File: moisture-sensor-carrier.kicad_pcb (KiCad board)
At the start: 4 copper layers, 42 x 155 mm, 61 parts, among them J1 USB-C receptacle, J2 Battery - Adafruit 1578, J3 Solar panel, J4 SWD 10p 1.27mm, J5 U.FL-R-SMT-1(10) antenna, U1 nRF54L15-QFAA, U2 nPM1300-QEAA, U3 FDC1004, U4 SHT45-AD1F, U5 TPS7A1650 5V LDO, X1 CM8V-T1A 32.768kHz CL=7pF 20p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, X2 FA-128 32MHz CL=8pF

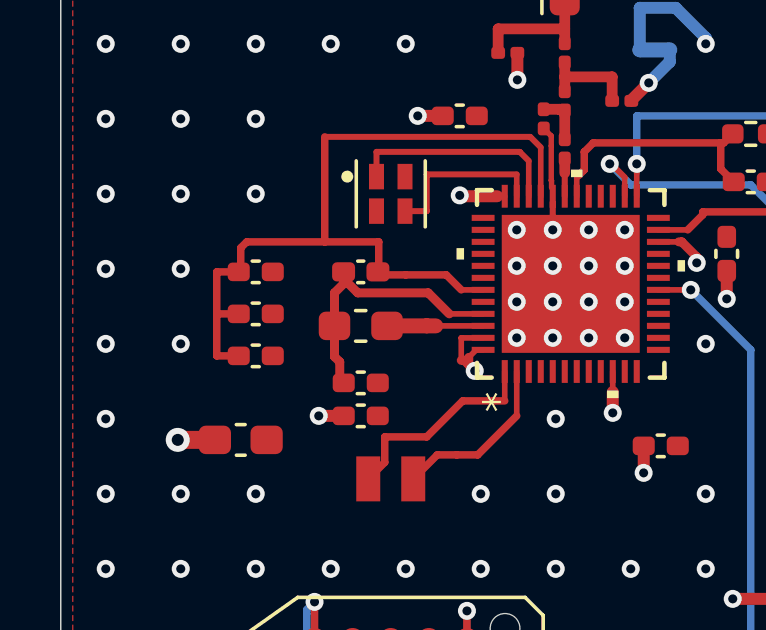
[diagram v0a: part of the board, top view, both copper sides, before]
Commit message: Pull the DECA bank in and give the decoupling local ground returns
Half the DECA bank's distance was free: C2, C12 and C5 all had their /DECA pad
on the WEST side, pointing AWAY from U1, so the net left each capacitor going
the wrong direction and doubled back. 1.13 mm each, for a rotation.

    C2   8.17 -> 6.04 mm      C12  8.19 -> 6.59      C5  8.44 -> 6.90

The eastward shift on top of that is small, and the reason is worth stating
rather than filing as a nudge: the band between the bank and the FB1/L1 column
is 0.67 mm, so each cap moved until its courtyard met its neighbour with
0.20 mm to spare. A 0402 hand-solder courtyard is 2.28 mm on its long axis and
the corridor between that column and U1 is 1.50 mm - no orientation of a 0402
fits there at all. Nordic packs these against the pins because their reference
uses 0201s. The remaining ~6 mm needs 0201s for this bank or a re-plan of the
whole west side of U1; it is not reachable by moving things.

The ground returns were reachable, and that fix is a via, not a move. The
stitching array is a 2.5 mm grid that knows nothing about where the decoupling
landed, so four caps returned through whatever via happened to be near:

    C1   4.87 -> 1.13 mm      C2  2.64 -> 0.93
    C12  2.60 -> 1.31         C5  2.44 -> 1.31

C1 is the DECD output cap, so its return carries the switching ripple, and it
was the longest leg of the nRF54L15 DC/DC loop by a wide margin.

The /DECA fan-out was rewritten for the new positions - it taps C2 first, the
closest of the three, then carries on to C12 and C5 instead of running out to
x = 65.20 and back.

DRC 1, 197 segments all on 45 degree multiples, DRU 20/20, netlist unchanged.

Co-Authored-By: Claude Opus 5 <noreply@anthropic.com>
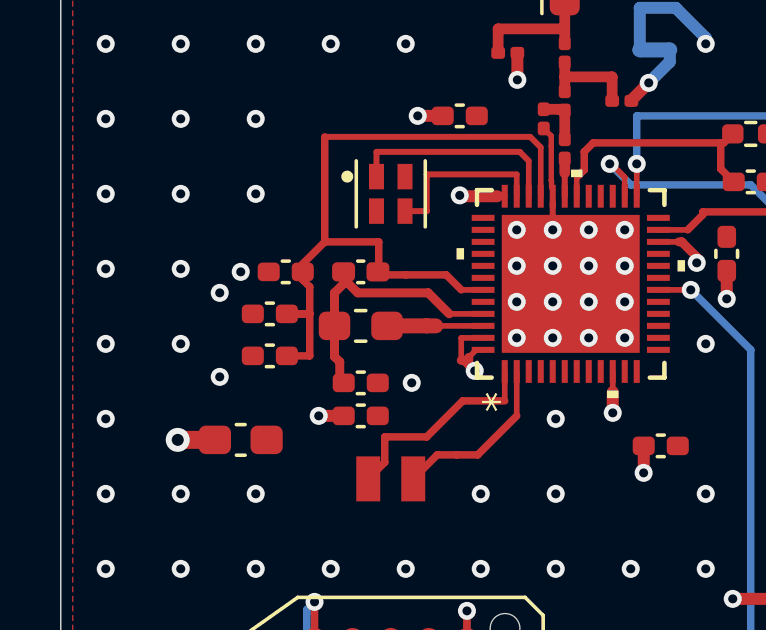
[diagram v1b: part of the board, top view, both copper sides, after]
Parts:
- moved C20 5.00 mm to (75.0, 91.5)
- moved C21 2.50 mm to (75.0, 94.0)
- moved C22 2.50 mm to (75.0, 96.5)
- moved C2 1.00 mm to (67.5, 62.6), turned to 180 degrees
- moved C12 0.47 mm to (67.0, 64.0), turned to 180 degrees
- moved C5 0.47 mm to (67.0, 65.4), turned to 180 degrees
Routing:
- net /DECA: track 27.7 -> 25.5 mm
- net GND: vias 138 -> 142

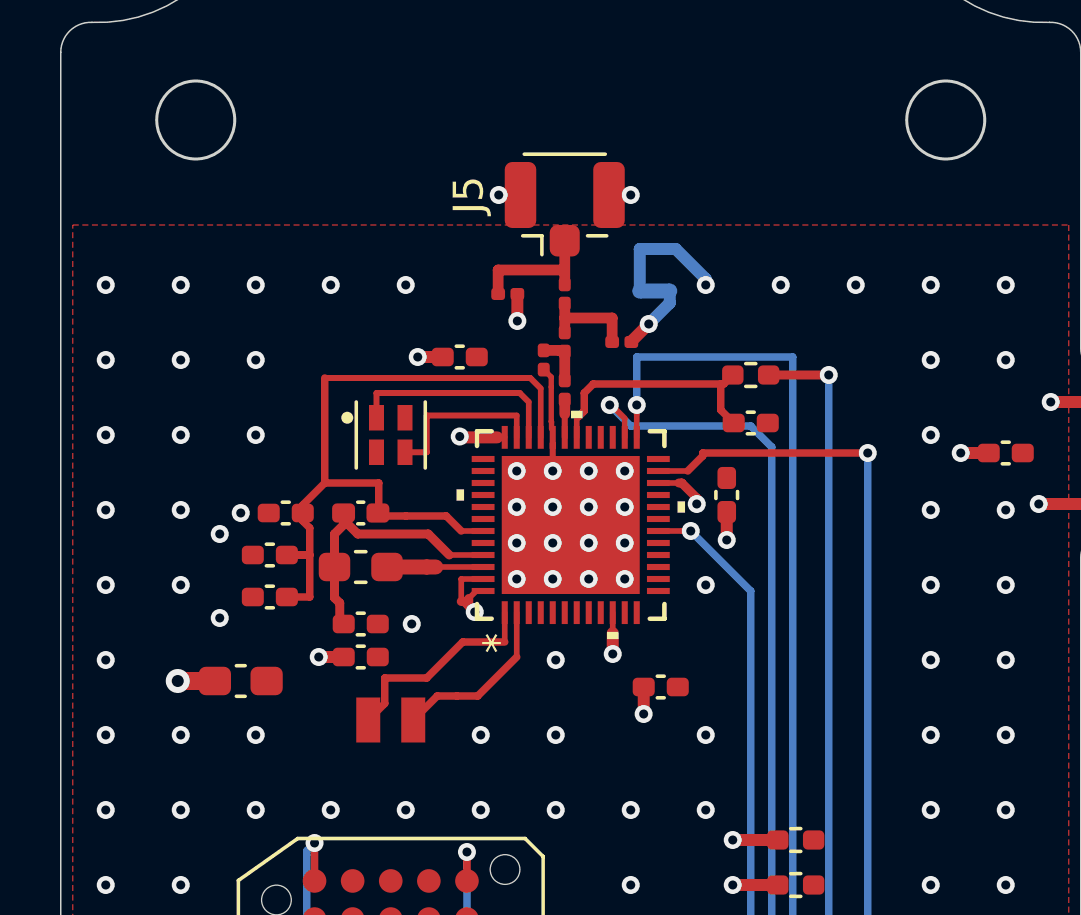
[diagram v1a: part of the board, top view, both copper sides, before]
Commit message: C9's shunt was an inductor. Give the RF return a plane, and turn C3 round.
C9 was NOT done, and the answer is not "ground it on the chip" - that is C6's
rule (pin 32 VSS_PA, reaching pin 49 only under the package, which /GND_PA and
NT1 already do). C9's rule is the opposite: reach ONLY the bottom ground layer,
isolated from every other.

The isolation was right. The via is on /GND_C9, so ZoneB_GND on In1.Cu clears
it. What was missing is the thing it was supposed to land on. Pages 3-5 of
Nordic's reference PCB show ground on L2, L3 AND L4 - two solid inner planes
and a poured bottom. This board has ground on In1.Cu only: In2.Cu is the 3V3
plane and B.Cu in Zone B was bare. So the previous commit ran the return ~5 mm
as a narrow B.Cu track to the nearest stitching via, and a narrow track is an
inductor:

    F.Cu stub 0.83 mm            0.50 nH
    through via F.Cu->B.Cu       1.34 nH
    B.Cu via -> NT2 1.30 mm      0.52 nH
    B.Cu NT2 -> stitch 4.20 mm   1.68 nH
    via B.Cu -> In1.Cu           1.15 nH
                                 ------- 5.18 nH = +j78.2 ohm at 2.4 GHz

against C9's own -j33.2. The shunt branch came out at +45 ohm - INDUCTIVE. A
2.0 pF shunt capacitor behaving as an inductor, which is the same failure the
C6 stub had and which that note calls "doing more to the match than the
capacitor".

ZoneB_GND_B is a B.Cu ground pour local to the RF return, so the via lands in
copper that spreads rather than a track that does not: 2.04 nH, +j30.7, branch
-2.5 ohm and still capacitive. The 4.20 mm detour is deleted.

It starts 1.20 mm east of the /ANT column, so it never sits under the RF trace
and the 50 ohm microstrip-over-In1.Cu geometry is untouched. Three existing
stitching vias tie it to In1.Cu, all at least 4.70 mm from the trace. The
inductance figures are estimates at 0.4-0.9 nH/mm - worth a VNA check at
bring-up with the rest of the match.

C3 had the DECA bank's problem: its +3V3 pad faced WEST at x = 65.138 while
U1.48 is at 74.079, so the rai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
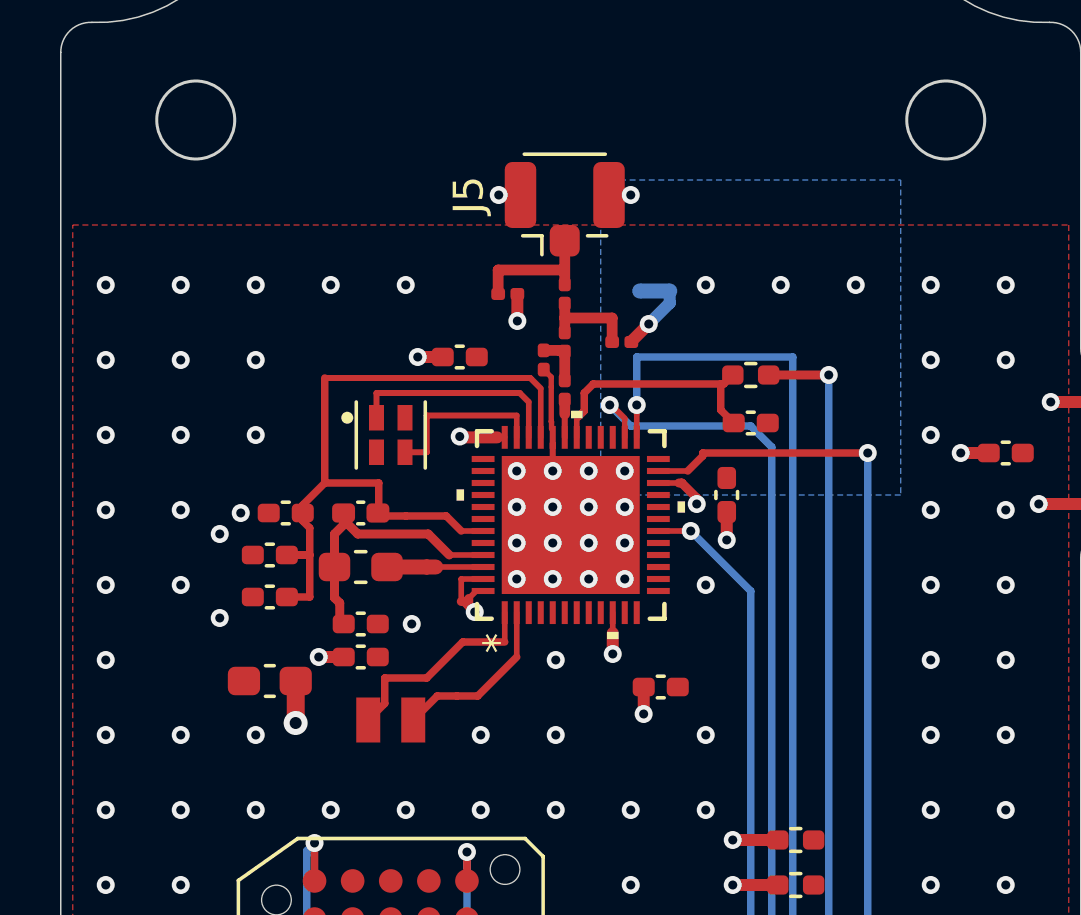
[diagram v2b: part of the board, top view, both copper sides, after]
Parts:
- moved C3 0.97 mm to (67.0, 68.2), turned to 180 degrees
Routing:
- net GND: track 18.7 -> 14.5 mm
- added copper zone on B.Cu, net GND
